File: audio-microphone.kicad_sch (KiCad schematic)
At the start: 9 parts, among them J1 JST_SH_1x4_BM04B-SRSS-TB-LF-SN

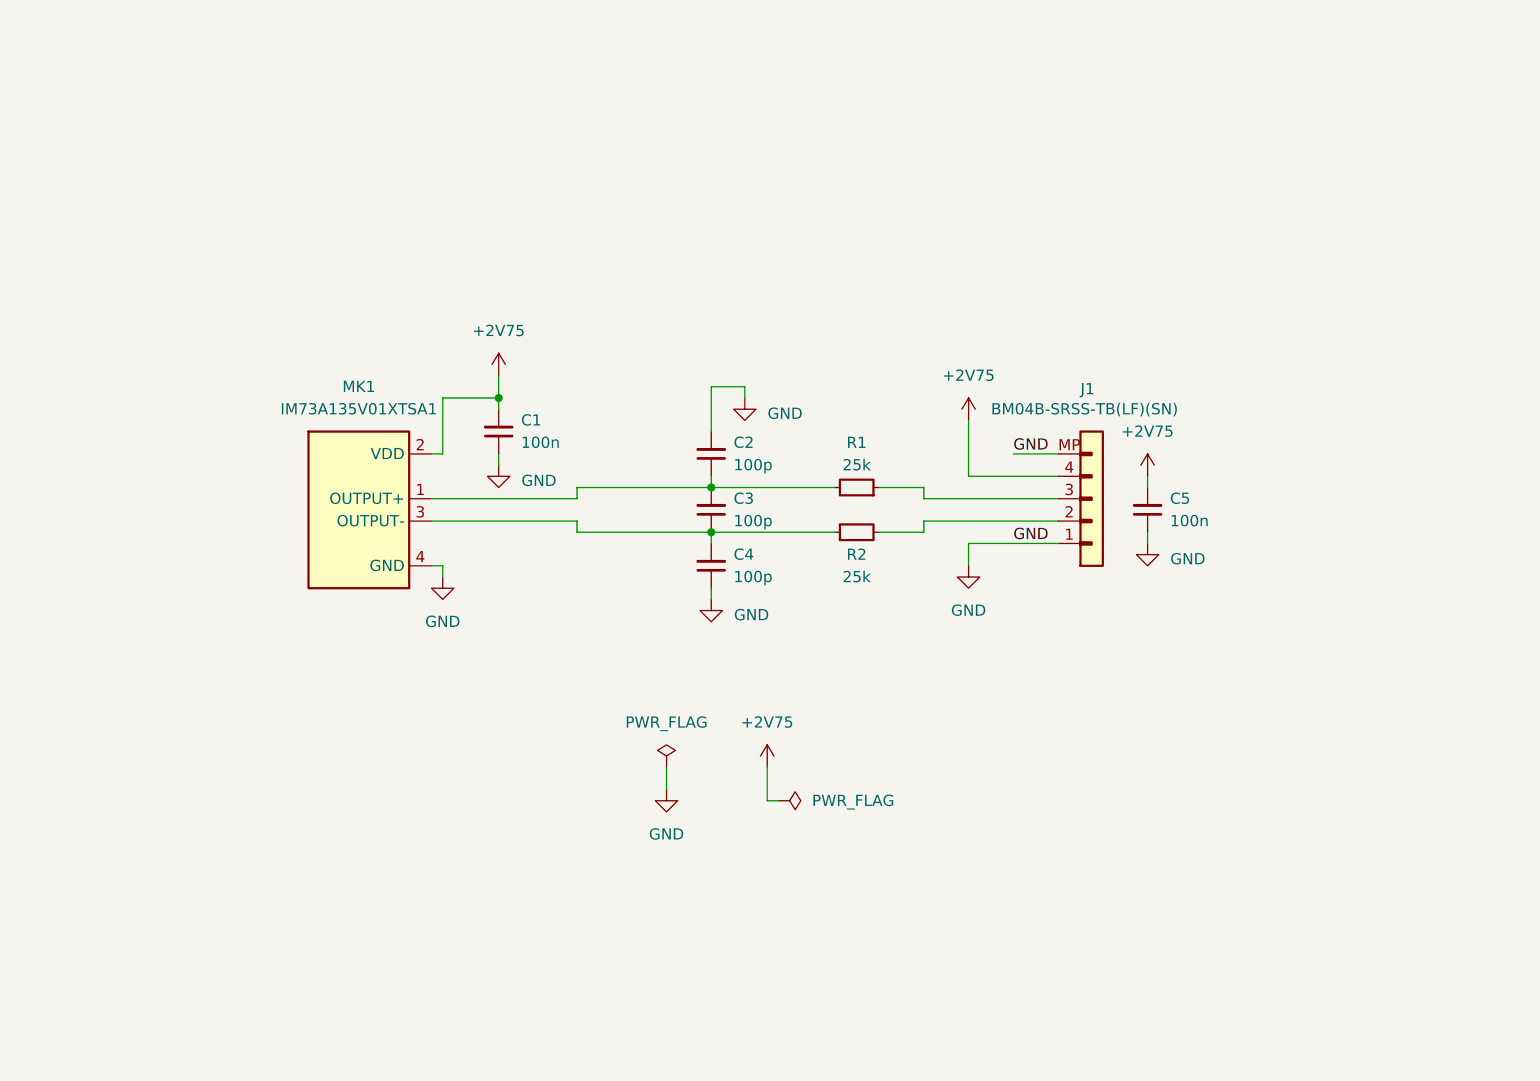
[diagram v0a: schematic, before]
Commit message: [#71550] Update sch with SPH0645LM4H-B mic
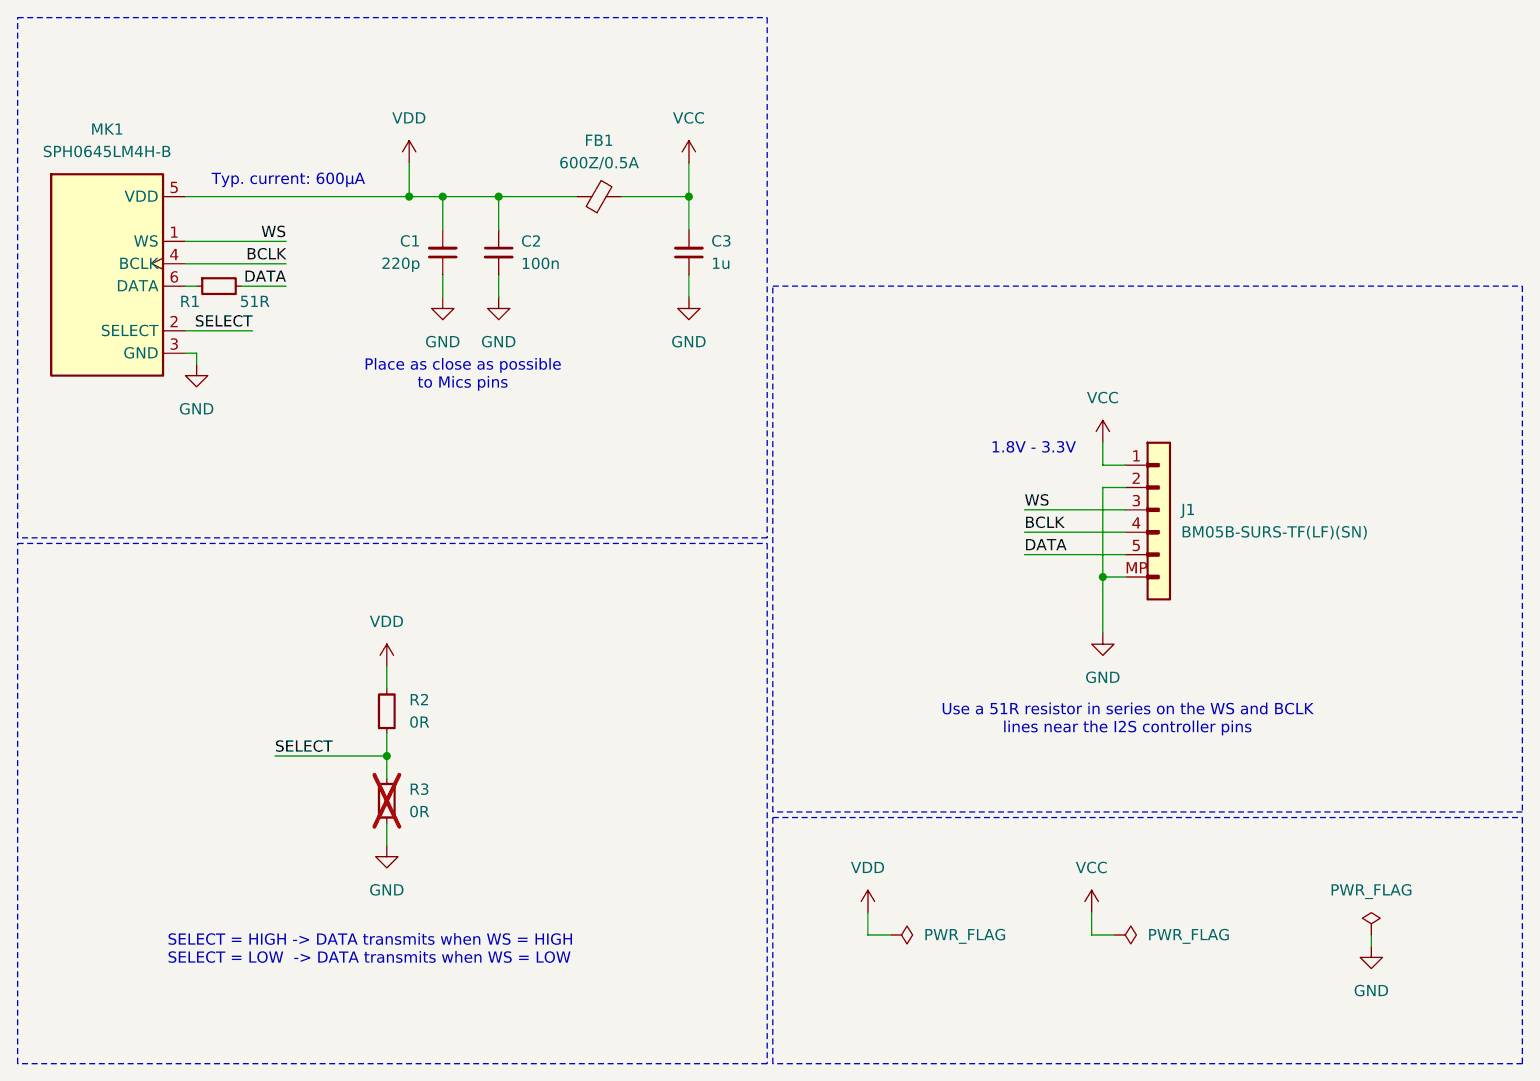
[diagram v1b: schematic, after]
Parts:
- removed C1, C5: C_100n_16V_X7R_0402, antmicro-footprints:C_0402_1005Metric, symbol antmicroCapacitors0402:C_100n_16V_X7R_0402
- removed C2, C3, C4: C_100p_0402, antmicro-footprints:C_0402_1005Metric, symbol antmicroCapacitors0402:C_100p_0402
- removed J1: JST_SH_1x4_BM04B-SRSS-TB-LF-SN, antmicro-footprints:Conn_JST_SH_1x4_BM04B-SRSS-TB-LF-SN, symbol antmicroWire2BoardConnectors:JST_SH_1x4_BM04B-SRSS-TB-LF-SN
- removed MK1: MK_IM73A135V01XTSA1, antmicro-footprints:MK_IM73A135V01XTSA1, symbol antmicroMicrophones:MK_IM73A135V01XTSA1
- removed R1, R2: R_25k_0402, antmicro-footprints:R_0402_1005Metric, symbol antmicroResistors0402:R_25k_0402
- added C1: C_220p_0402, antmicro-footprints:C_0402_1005Metric, symbol antmicroCapacitors0402:C_220p_0402
- added C2: C_100n_0402, antmicro-footprints:C_0402_1005Metric, symbol antmicroCapacitors0402:C_100n_0402
- added C3: C_1u_0402, antmicro-footprints:C_0402_1005Metric, symbol antmicroCapacitors0402:C_1u_0402
- added FB1: FB_600Z_0.5A_Murata-BLM18AG_0603, antmicro-footprints:FB_0603_1608Metric, symbol antmicroFerriteBeadsandChips:FB_600Z_0.5A_Murata-BLM18AG_0603
- added J1: JST_SH_1x5_BM05B-SURS-TB-LF-SN, antmicro-footprints:Conn_JST_SH_1x5_BM05B-SURS-TF-LF-SN, symbol antmicroWire2BoardConnectors:JST_SH_1x5_BM05B-SURS-TB-LF-SN
- added MK1: MK_SPH0645LM4H-B, antmicro-footprints:MK_SPH0645LM4H-B, symbol antmicroMicrophones:MK_SPH0645LM4H-B
- added R1: R_51R_0402, antmicro-footprints:R_0402_1005Metric, symbol antmicroResistors0402:R_51R_0402
- added R2, R3: R_0R_0402, antmicro-footprints:R_0402_1005Metric, symbol antmicroResistors0402:R_0R_0402
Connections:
- net GND: now also C1.1, C2.2, C3.1, J1.2, J1.MP, MK1.3 (GND), R3.1
- new net: MK1.6 (DATA), R1.1
- new net BCLK: J1.4, MK1.4 (BCLK)
- new net DATA: J1.5, R1.2
- new net SELECT: MK1.2 (SELECT), R2.1, R3.2
- new net VCC: C3.2, FB1.2, J1.1
- new net VDD: C1.2, C2.1, FB1.1, MK1.5 (VDD), R2.2
- new net WS: J1.3, MK1.1 (WS)
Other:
- note added: "1.8V - 3.3V"
- note added: "Place as close as possible to Mics pins"
- note added: "SELECT = HIGH -> DATA transmits when WS = HIGH SELECT = LOW -> DATA transmits when WS = LOW"
- note added: "Typ. current: 600µA"
- note added: "Use a 51R resistor in series on the WS and BCLK lines near the I2S controller pins"

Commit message: [#71550] Route connections
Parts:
- removed J1: JST_SH_1x5_BM05B-SURS-TB-LF-SN, antmicro-footprints:Conn_JST_SH_1x5_BM05B-SURS-TF-LF-SN, symbol antmicroWire2BoardConnectors:JST_SH_1x5_BM05B-SURS-TB-LF-SN
- added J1: JST_SUR_1x5_BM05B-SURS-TB-LF-SN, antmicro-footprints:Conn_JST_SUR_1x5_BM05B-SURS-TF-LF-SN, symbol antmicroWire2BoardConnectors:JST_SUR_1x5_BM05B-SURS-TB-LF-SN
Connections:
- net BCLK: now also J1.4
- net DATA: now also J1.5
- net GND: now also J1.2, J1.MP
- net VCC: now also J1.1
- net WS: now also J1.3
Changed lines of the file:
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@@
+	)
+	(symbol
+		(lib_id "antmicroWire2BoardConnectors:JST_SUR_1x5_BM05B-SURS-TB-LF-SN")
+		(at 194.31 90.17 0)
+		(unit 1)
+		(exclude_from_sim no)
+		(in_bom yes)
+		(on_board yes)
+		(dnp no)
+		(fields_autoplaced yes)
+		(property "Reference" "J1"
+			(at 200.66 95.25 0)
+			(effects
+				(font
+					(size 1.27 1.27)
+					(thickness 0.15)
+				)
+				(justify left)
+			)
+		)
+		(property "Value" "JST_SUR_1x5_BM05B-SURS-TB-LF-SN"
+			(at 214.63 97.79 0)
+			(effects
+				(font
+					(size 1.27 1.27)
+					(thickness 0.15)
+				)
+				(justify left bottom)
+				(hide yes)
+			)
+		)
+		(property "Footprint" "antmicro-footprints:Conn_JST_SUR_1x5_BM05B-SURS-TF-LF-SN"
+			(at 214.63 100.33 0)
+			(effects
+				(font
+					(size 1.27 1.27)
+					(thickness 0.15)
+				)
+				(justify left bottom)
+				(hide yes)
+			)
+		)
+		(property "Datasheet" "https://www.jst.com/wp-content/uploads/2021/09/eSUR-new.pdf"
+			(at 214.63 102.87 0)
+			(effects
+				(font
+					(size 1.27 1.27)
+					(thickness 0.15)
+				)
+				(justify left bottom)
+				(hide yes)
+			)
+		)
+		(property "Description" "Pin Header, Vertical, Wire-to-Board, 0.5 mm, 1 Rows, 5 Contacts, Surface Mount Vertical, SUR"
+			(at 214.63 105.41 0)
+			(effects
+				(font
+					(size 1.27 1.27)
+					(thickness 0.15)
+				)
+				(justify left bottom)
+				(hide yes)
+			)
+		)
+		(property "MPN" " BM05B-SURS-TF(LF)(SN)"
+			(at 200.66 97.79 0)
+			(effects
+				(font
+					(size 1.27 1.27)
+					(thickness 0.15)
+				)
+				(justify left)
+			)
+		)
+		(property "Manufacturer" "JST Automotive Connectors"
+			(at 214.63 107.95 0)
+			(effects
+				(font
+					(size 1.27 1.27)
+					(thickness 0.15)
+				)
+				(justify left bottom)
+				(hide yes)
+			)
+		)
+		(property "Author" "Antmicro"
+			(at 214.63 110.49 0)
+			(effects
+				(font
+					(size 1.27 1.27)
+					(thickness 0.15)
+				)
+				(justify left bottom)
+				(hide yes)
+			)
+		)
+		(property "License" "Apache-2.0"
+			(at 214.63 113.03 0)
+			(effects
+				(font
+					(size 1.27 1.27)
+					(thickness 0.15)
+				)
+				(justify left bottom)
+				(hide yes)
+			)
+		)
+		(pin "2"
+		)
+		(pin "3"
+		)
+		(pin "1"
+		)
+		(pin "4"
+		)
+		(pin "5"
+		)
+		(pin "MP"
+		)
+		(instances
+			(project ""
+				(path "/4a2cf8c5-6ba3-448d-b2e4-bea2166340e3"
+					(reference "J1")
+					(unit 1)
+				)
+			)
+		)
 	)
 	(symbol
@@
 					(unit 1)
 				)
-			)
-		)
-	)
-	(symbol
-		(lib_id "antmicroWire2BoardConnectors:JST_SH_1x5_BM05B-SURS-TB-LF-SN")
-		(at 194.31 90.17 0)
-		(unit 1)
-		(exclude_from_sim no)
-		(in_bom yes)
-		(on_board yes)
-		(dnp no)
-		(fields_autoplaced yes)
-		(property "Reference" "J1"
-			(at 200.66 95.25 0)
-			(effects
-				(font
-					(size 1.27 1.27)
-					(thickness 0.15)
-				)
-				(justify left)
-			)
-		)
-		(property "Value" "JST_SH_1x5_BM05B-SURS-TB-LF-SN"
-			(at 214.63 97.79 0)
-			(effects
-				(font
-					(size 1.27 1.27)
-					(thickness 0.15)
-				)
-				(justify left bottom)
-				(hide yes)
-			)
-		)
-		(property "Footprint" "antmicro-footprints:Conn_JST_SH_1x5_BM05B-SURS-TF-LF-SN"
-			(at 214.63 100.33 0)
-			(effects
-				(font
-					(size 1.27 1.27)
-					(thickness 0.15)
-				)
-				(justify left bottom)
-				(hide yes)
-			)
-		)
-		(property "Datasheet" "https://www.jst.com/wp-content/uploads/2021/09/eSUR-new.pdf"
-			(at 214.63 102.87 0)
-			(effects
-				(font
-					(size 1.27 1.27)
-					(thickness 0.15)
-				)
-				(justify left bottom)
-				(hide yes)
-			)
-		)
-		(property "Description" "Pin Header, Vertical, Wire-to-Board, 0.5 mm, 1 Rows, 5 Contacts, Surface Mount Vertical, SUR"
-			(at 214.63 105.41 0)
-			(effects
-				(font
-					(size 1.27 1.27)
-					(thickness 0.15)
-				)
-				(justify left bottom)
-				(hide yes)
-			)
-		)
-		(property "MPN" " BM05B-SURS-TF(LF)(SN)"
-			(at 200.66 97.79 0)
-			(effects
-				(font
-					(size 1.27 1.27)
-					(thickness 0.15)
-				)
-				(justify left)
-			)
-		)
-		(property "Manufacturer" "JST Automotive Connectors"
-			(at 214.63 107.95 0)
-			(effects
-				(font
-					(size 1.27 1.27)
-					(thickness 0.15)
-				)
-				(justify left bottom)
-				(hide yes)
-			)
-		)
-		(property "Author" "Antmicro"
-			(at 214.63 110.49 0)
-			(effects
-				(font
-					(size 1.27 1.27)
-					(thickness 0.15)
-				)
-				(justify left bottom)
-				(hide yes)
-			)
-		)
-		(property "License" "Apache-2.0"
-			(at 214.63 113.03 0)
-			(effects
-				(font
-					(size 1.27 1.27)
-					(thickness 0.15)
-				)
-				(justify left bottom)
-				(hide yes)
-			)
-		)
-		(pin "1"
-		)
-		(pin "MP"
-		)
-		(pin "5"
-		)
-		(pin "2"
-		)
-		(pin "3"
-		)
-		(pin "4"
-		)
-		(instances
-			(project ""
-				(path "/4a2cf8c5-6ba3-448d-b2e4-bea2166340e3"
-					(reference "J1")
-					(unit 1)
-				)

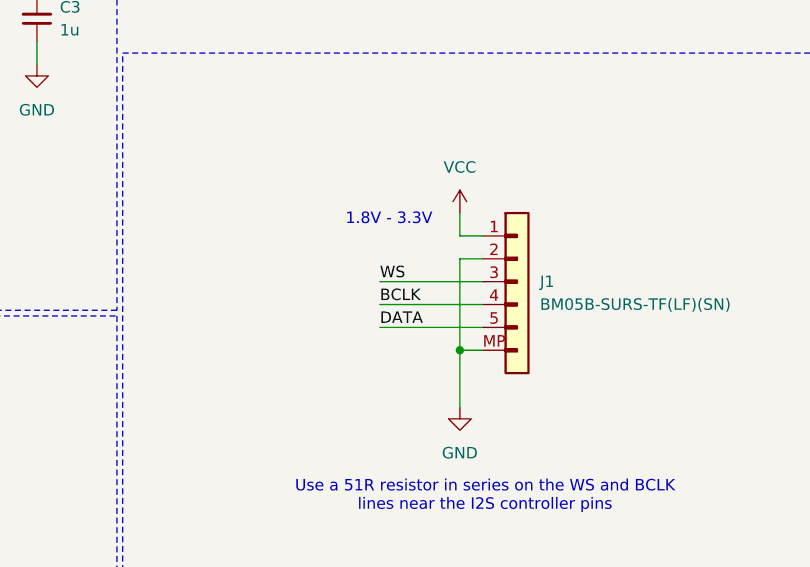
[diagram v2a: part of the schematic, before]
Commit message: [#71550] Swap BCLK and WS, Fix outline
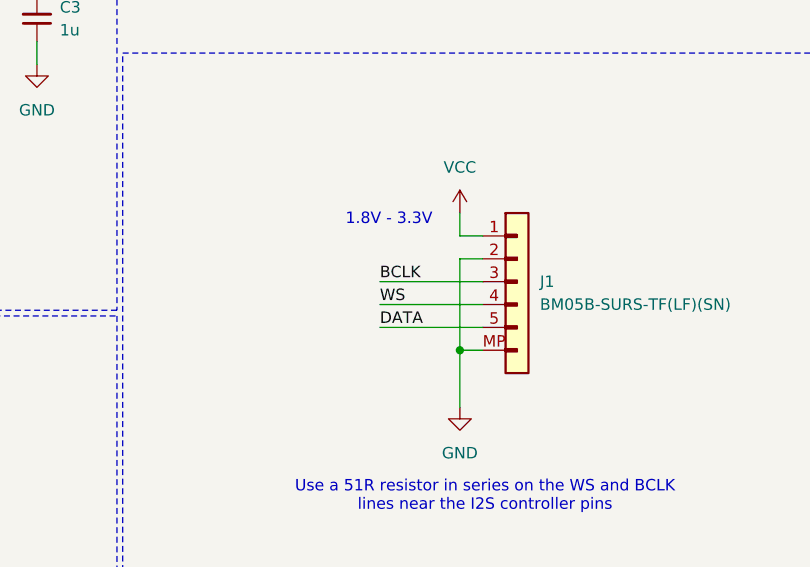
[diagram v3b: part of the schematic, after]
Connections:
- net BCLK: now also J1.3; no longer J1.4
- net WS: now also J1.4; no longer J1.3
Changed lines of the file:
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@@
 	)
 	(label "WS"
-		(at 182.88 95.25 0)
+		(at 182.88 97.79 0)
 		(fields_autoplaced yes)
 		(effects
@@
 	)
 	(label "BCLK"
-		(at 182.88 97.79 0)
+		(at 182.88 95.25 0)
 		(fields_autoplaced yes)
 		(effects
